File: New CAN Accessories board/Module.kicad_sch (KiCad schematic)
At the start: 11 parts, among them J1 39301040, Q1 IRLML6344TRPBF

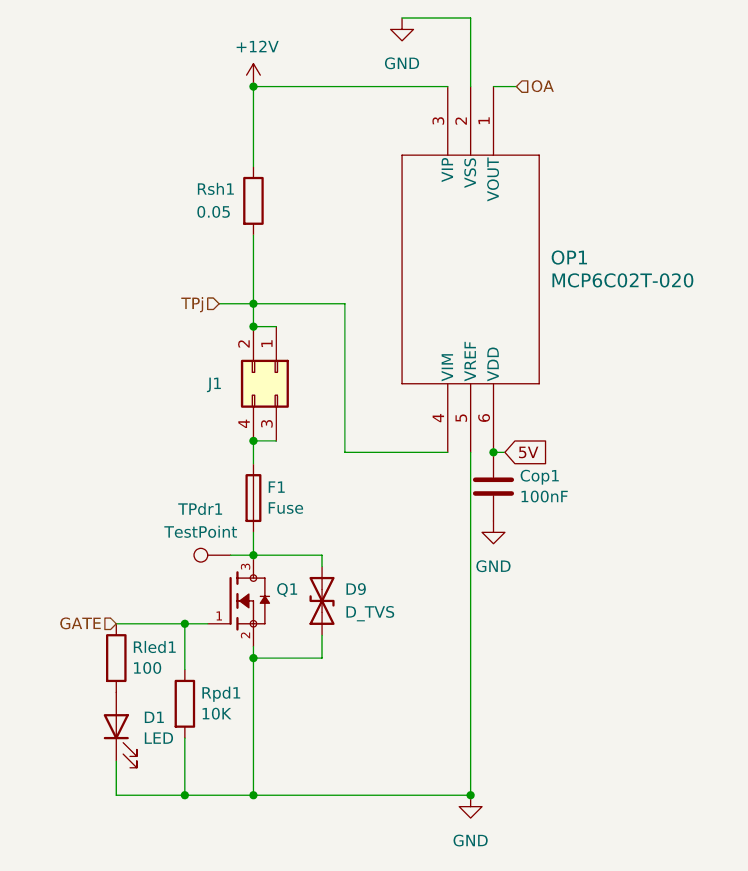
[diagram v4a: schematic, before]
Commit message: named tvs diode correctly
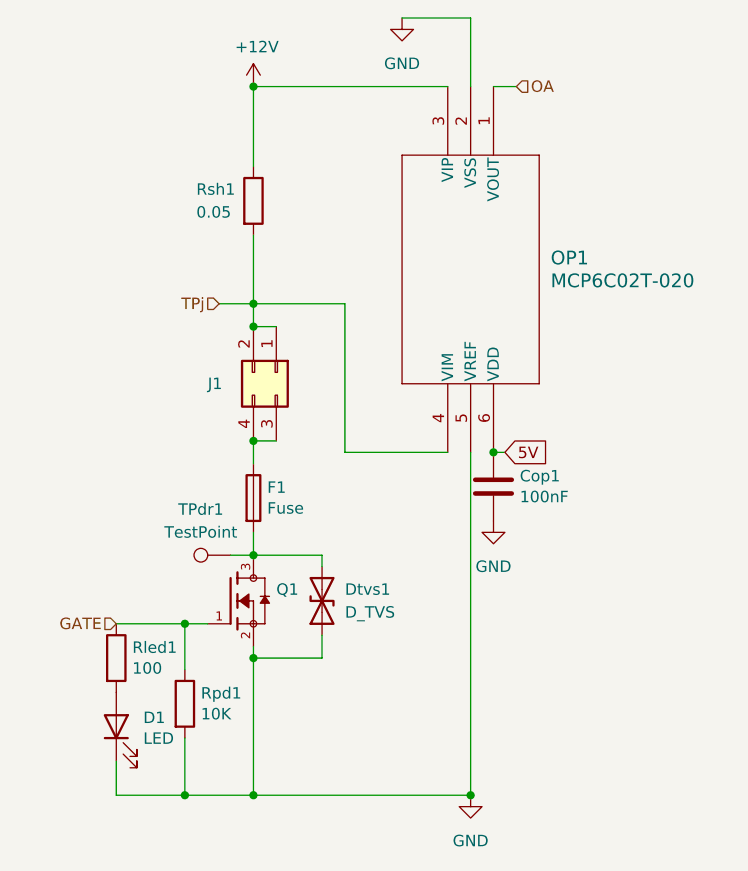
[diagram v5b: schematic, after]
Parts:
- removed D9: D_TVS, symbol Device:D_TVS
- added Dtvs1: D_TVS, symbol Device:D_TVS
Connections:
- net GND: now also Dtvs1.1 (A1)
- net at F1.2, Q1.3, TPdr1.1: now also Dtvs1.2 (A2)
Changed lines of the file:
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@@
-	(wire
-		(pts
-			(xy 48.26 76.2) (xy 48.26 77.47)
-		)
-		(stroke
-			(width 0)
-			(type default)
-		)
-	)
 	(wire
 		(pts
@@
 		(pts
 			(xy 48.26 85.09) (xy 48.26 87.63)
+		)
+		(stroke
+			(width 0)
+			(type default)
+		)
+	)
+	(wire
+		(pts
+			(xy 48.26 77.47) (xy 48.26 76.2)
 		)
 		(stroke
@@
 	)
 	(symbol
+		(lib_id "Device:D_TVS")
+		(at 48.26 81.28 90)
+		(unit 1)
+		(exclude_from_sim no)
+		(in_bom yes)
+		(on_board yes)
+		(dnp no)
+		(fields_autoplaced yes)
+		(property "Reference" "Dtvs1"
+			(at 50.8 80.0099 90)
+			(effects
+				(font
+					(size 1.27 1.27)
+				)
+				(justify right)
+			)
+		)
+		(property "Value" "D_TVS"
+			(at 50.8 82.5499 90)
+			(effects
+				(font
+					(size 1.27 1.27)
+				)
+				(justify right)
+			)
+		)
+		(property "Footprint" ""
+			(at 48.26 81.28 0)
+			(effects
+				(font
+					(size 1.27 1.27)
+				)
+				(hide yes)
+			)
+		)
+		(property "Datasheet" "~"
+			(at 48.26 81.28 0)
+			(effects
+				(font
+					(size 1.27 1.27)
+				)
+				(hide yes)
+			)
+		)
+		(property "Description" "Bidirectional transient-voltage-suppression diode"
+			(at 48.26 81.28 0)
+			(effects
+				(font
+					(size 1.27 1.27)
+				)
+				(hide yes)
+			)
+		)
+		(pin "2"
+		)
+		(pin "1"
+		)
+		(instances
+			(project "New CAN Accessories board"
+				(path "/88340f43-3f46-45a6-9393-130e00dc3071/066a2d54-ef62-4b50-bc17-9ae15f85282f"
+					(reference "Dtvs3")
+					(unit 1)
+				)
+				(path "/88340f43-3f46-45a6-9393-130e00dc3071/199d9661-d77c-40a8-9127-2f77ddd20cbc"
+					(reference "Dtvs2")
+					(unit 1)
+				)
+				(path "/88340f43-3f46-45a6-9393-130e00dc3071/a4a3a29c-d4d7-4a64-89ca-c4c515902e3a"
+					(reference "Dtvs8")
+					(unit 1)
+				)
+				(path "/88340f43-3f46-45a6-9393-130e00dc3071/b4fef664-0317-4528-b914-9a729a4fa0cb"
+					(reference "Dtvs7")
+					(unit 1)
+				)
+				(path "/88340f43-3f46-45a6-9393-130e00dc3071/df424b4d-8c7c-4d94-be97-d7e7a5882dfa"
+					(reference "Dtvs6")
+					(unit 1)
+				)
+				(path "/88340f43-3f46-45a6-9393-130e00dc3071/e28dd46e-a6b0-42fd-b358-90f6a987ac56"
+					(reference "Dtvs4")
+					(unit 1)
+				)
+				(path "/88340f43-3f46-45a6-9393-130e00dc3071/f4946d2d-97a8-44f8-9d9c-ff737967b4cd"
+					(reference "Dtvs5")
+					(unit 1)
+				)
+				(path "/88340f43-3f46-45a6-9393-130e00dc3071/fb19124a-c234-4595-adc5-bbb1e37c8292"
+					(reference "Dtvs1")
+					(unit 1)
+				)
+			)
+		)
+	)
+	(symbol
 		(lib_id "Device:R")
 		(at 33.02 92.71 0)
@@
 					(unit 1)
 				)
-			)
-		)
-	)
-	(symbol
-		(lib_id "Device:D_TVS")
-		(at 48.26 81.28 90)
-		(unit 1)
-		(exclude_from_sim no)
-		(in_bom yes)
-		(on_board yes)
-		(dnp no)
-		(fields_autoplaced yes)
-		(property "Reference" "D9"
-			(at 50.8 80.0099 90)
-			(effects
-				(font
-					(size 1.27 1.27)
-				)
-				(justify right)
-			)
-		)
-		(property "Value" "D_TVS"
-			(at 50.8 82.5499 90)
-			(effects
-				(font
-					(size 1.27 1.27)
-				)
-				(justify right)
-			)
-		)
-		(property "Footprint" ""
-			(at 48.26 81.28 0)
-			(effects
-				(font
-					(size 1.27 1.27)
-				)
-				(hide yes)
-			)
-		)
-		(property "Datasheet" "~"
-			(at 48.26 81.28 0)
-			(effects
-				(font
-					(size 1.27 1.27)
-				)
-				(hide yes)
-			)
-		)
-		(property "Description" "Bidirectional transient-voltage-suppression diode"
-			(at 48.26 81.28 0)
-			(effects
-				(font
-					(size 1.27 1.27)
-				)
-				(hide yes)
-			)
-		)
-		(pin "1"
-		)
-		(pin "2"
-		)
-		(instances
-			(project ""
-				(path "/88340f43-3f46-45a6-9393-130e00dc3071/066a2d54-ef62-4b50-bc17-9ae15f85282f"
-					(reference "D11")
-					(unit 1)
-				)
-				(path "/88340f43-3f46-45a6-9393-130e00dc3071/199d9661-d77c-40a8-9127-2f77ddd20cbc"
-					(reference "D10")
-					(unit 1)
-				)
-				(path "/88340f43-3f46-45a6-9393-130e00dc3071/a4a3a29c-d4d7-4a64-89ca-c4c515902e3a"
-					(reference "D16")
-					(unit 1)
-				)
-				(path "/88340f43-3f46-45a6-9393-130e00dc3071/b4fef664-0317-4528-b914-9a729a4fa0cb"
-					(reference "D15")
-					(unit 1)
-				)
-				(path "/88340f43-3f46-45a6-9393-130e00dc3071/df424b4d-8c7c-4d94-be97-d7e7a5882dfa"
-					(reference "D14")
-					(unit 1)
-				)
-				(path "/88340f43-3f46-45a6-9393-130e00dc3071/e28dd46e-a6b0-42fd-b358-90f6a987ac56"
-					(reference "D12")
-					(unit 1)
-				)
-				(path "/88340f43-3f46-45a6-9393-130e00dc3071/f4946d2d-97a8-44f8-9d9c-ff737967b4cd"
-					(reference "D13")
-					(unit 1)
-				)
-				(path "/88340f43-3f46-45a6-9393-130e00dc3071/fb19124a-c234-4595-adc5-bbb1e37c8292"
-					(reference "D9")
-					(unit 1)
-				)

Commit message: started making drain test point changes
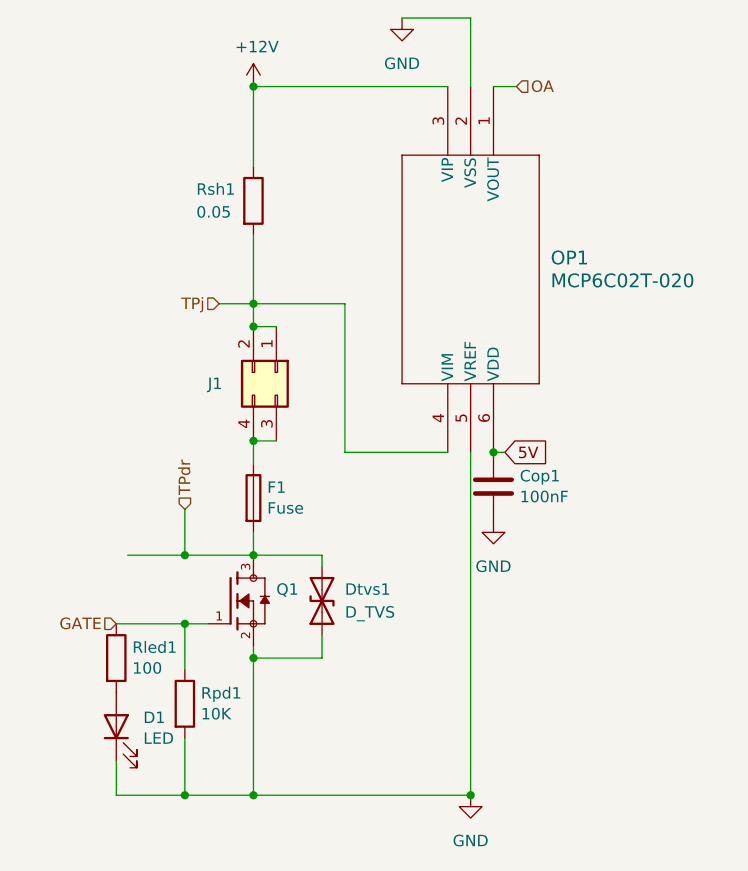
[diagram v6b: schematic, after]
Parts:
- removed TPdr1: TestPoint, Connector_PinHeader_2.54mm:PinHeader_1x01_P2.54mm_Vertical, symbol Connector:TestPoint
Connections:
- net TPdr: now reaches Dtvs1.2 (A2), F1.2, Q1.3
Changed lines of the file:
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@@
+	)
+	(junction
+		(at 33.02 76.2)
+		(diameter 0)
+		(color 0 0 0 0)
 	)
 	(junction
@@
 	(wire
 		(pts
+			(xy 33.02 76.2) (xy 40.64 76.2)
+		)
+		(stroke
+			(width 0)
+			(type default)
+		)
+	)
+	(wire
+		(pts
 			(xy 50.8 48.26) (xy 40.64 48.26)
 		)
@@
 	(wire
 		(pts
-			(xy 38.1 76.2) (xy 40.64 76.2)
+			(xy 26.67 76.2) (xy 33.02 76.2)
+		)
+		(stroke
+			(width 0)
+			(type default)
+		)
+	)
+	(wire
+		(pts
+			(xy 33.02 71.12) (xy 33.02 76.2)
 		)
 		(stroke
@@
 				(hide yes)
 			)
+		)
+	)
+	(hierarchical_label "TPdr"
+		(shape input)
+		(at 33.02 71.12 90)
+		(effects
+			(font
+				(size 1.27 1.27)
+			)
+			(justify left)
 		)
 	)
@@
 					(unit 1)
 				)
-			)
-		)
-	)
-	(symbol
-		(lib_id "Connector:TestPoint")
-		(at 38.1 76.2 90)
-		(unit 1)
-		(exclude_from_sim no)
-		(in_bom yes)
-		(on_board yes)
-		(dnp no)
-		(fields_autoplaced yes)
-		(property "Reference" "TPdr1"
-			(at 34.798 71.12 90)
-			(effects
-				(font
-					(size 1.27 1.27)
-				)
-			)
-		)
-		(property "Value" "TestPoint"
-			(at 34.798 73.66 90)
-			(effects
-				(font
-					(size 1.27 1.27)
-				)
-			)
-		)
-		(property "Footprint" "Connector_PinHeader_2.54mm:PinHeader_1x01_P2.54mm_Vertical"
-			(at 38.1 71.12 0)
-			(effects
-				(font
-					(size 1.27 1.27)
-				)
-				(hide yes)
-			)
-		)
-		(property "Datasheet" "~"
-			(at 38.1 71.12 0)
-			(effects
-				(font
-					(size 1.27 1.27)
-				)
-				(hide yes)
-			)
-		)
-		(property "Description" "test point"
-			(at 38.1 76.2 0)
-			(effects
-				(font
-					(size 1.27 1.27)
-				)
-				(hide yes)
-			)
-		)
-		(property "Purpose" ""
-			(at 38.1 76.2 0)
-			(effects
-				(font
-					(size 1.27 1.27)
-				)
-			)
-		)
-		(pin "1"
-		)
-		(instances
-			(project "New CAN Accessories board"
-				(path "/88340f43-3f46-45a6-9393-130e00dc3071/066a2d54-ef62-4b50-bc17-9ae15f85282f"
-					(reference "TPdr3")
-					(unit 1)
-				)
-				(path "/88340f43-3f46-45a6-9393-130e00dc3071/199d9661-d77c-40a8-9127-2f77ddd20cbc"
-					(reference "TPdr2")
-					(unit 1)
-				)
-				(path "/88340f43-3f46-45a6-9393-130e00dc3071/a4a3a29c-d4d7-4a64-89ca-c4c515902e3a"
-					(reference "TPdr8")
-					(unit 1)
-				)
-				(path "/88340f43-3f46-45a6-9393-130e00dc3071/b4fef664-0317-4528-b914-9a729a4fa0cb"
-					(reference "TPdr7")
-					(unit 1)
-				)
-				(path "/88340f43-3f46-45a6-9393-130e00dc3071/df424b4d-8c7c-4d94-be97-d7e7a5882dfa"
-					(reference "TPdr6")
-					(unit 1)
-				)
-				(path "/88340f43-3f46-45a6-9393-130e00dc3071/e28dd46e-a6b0-42fd-b358-90f6a987ac56"
-					(reference "TPdr4")
-					(unit 1)
-				)
-				(path "/88340f43-3f46-45a6-9393-130e00dc3071/f4946d2d-97a8-44f8-9d9c-ff737967b4cd"
-					(reference "TPdr5")
-					(unit 1)
-				)
-				(path "/88340f43-3f46-45a6-9393-130e00dc3071/fb19124a-c234-4595-adc5-bbb1e37c8292"
-					(reference "TPdr1")
-					(unit 1)
-				)

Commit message: 1x16 header test points
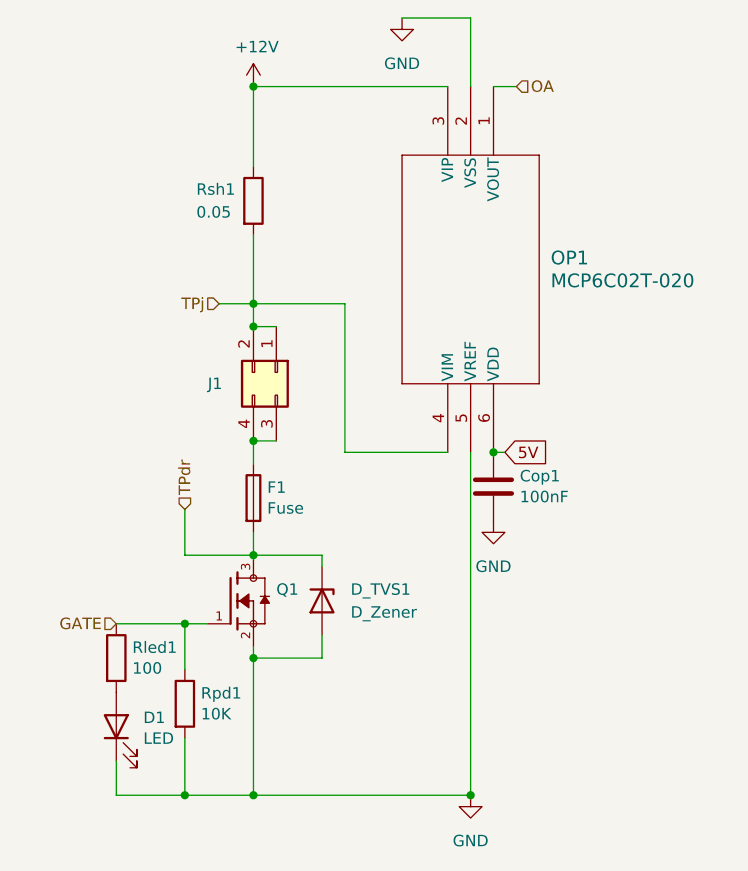
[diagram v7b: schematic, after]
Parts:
- removed Dtvs1: D_TVS, symbol Device:D_TVS
- added D_TVS1: D_Zener, Diode_SMD:D_SMF, symbol Device:D_Zener
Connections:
- net GND: now also D_TVS1.2 (A)
- net TPdr: now also D_TVS1.1 (K)
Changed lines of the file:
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@@
-	)
-	(junction
-		(at 33.02 76.2)
-		(diameter 0)
-		(color 0 0 0 0)
 	)
 	(junction
@@
 		(pts
 			(xy 69.85 24.13) (xy 67.31 24.13)
-		)
-		(stroke
-			(width 0)
-			(type default)
-		)
-	)
-	(wire
-		(pts
-			(xy 26.67 76.2) (xy 33.02 76.2)
 		)
 		(stroke
@@
 	)
 	(symbol
-		(lib_id "Device:D_TVS")
-		(at 48.26 81.28 90)
-		(unit 1)
-		(exclude_from_sim no)
-		(in_bom yes)
-		(on_board yes)
-		(dnp no)
-		(fields_autoplaced yes)
-		(property "Reference" "Dtvs1"
-			(at 50.8 80.0099 90)
-			(effects
-				(font
-					(size 1.27 1.27)
-				)
-				(justify right)
-			)
-		)
-		(property "Value" "D_TVS"
-			(at 50.8 82.5499 90)
-			(effects
-				(font
-					(size 1.27 1.27)
-				)
-				(justify right)
-			)
-		)
-		(property "Footprint" ""
-			(at 48.26 81.28 0)
-			(effects
-				(font
-					(size 1.27 1.27)
-				)
-				(hide yes)
-			)
-		)
-		(property "Datasheet" "~"
-			(at 48.26 81.28 0)
-			(effects
-				(font
-					(size 1.27 1.27)
-				)
-				(hide yes)
-			)
-		)
-		(property "Description" "Bidirectional transient-voltage-suppression diode"
-			(at 48.26 81.28 0)
-			(effects
-				(font
-					(size 1.27 1.27)
-				)
-				(hide yes)
-			)
-		)
-		(pin "2"
-		)
-		(pin "1"
-		)
-		(instances
-			(project "New CAN Accessories board"
-				(path "/88340f43-3f46-45a6-9393-130e00dc3071/066a2d54-ef62-4b50-bc17-9ae15f85282f"
-					(reference "Dtvs3")
-					(unit 1)
-				)
-				(path "/88340f43-3f46-45a6-9393-130e00dc3071/199d9661-d77c-40a8-9127-2f77ddd20cbc"
-					(reference "Dtvs2")
-					(unit 1)
-				)
-				(path "/88340f43-3f46-45a6-9393-130e00dc3071/a4a3a29c-d4d7-4a64-89ca-c4c515902e3a"
-					(reference "Dtvs8")
-					(unit 1)
-				)
-				(path "/88340f43-3f46-45a6-9393-130e00dc3071/b4fef664-0317-4528-b914-9a729a4fa0cb"
-					(reference "Dtvs7")
-					(unit 1)
-				)
-				(path "/88340f43-3f46-45a6-9393-130e00dc3071/df424b4d-8c7c-4d94-be97-d7e7a5882dfa"
-					(reference "Dtvs6")
-					(unit 1)
-				)
-				(path "/88340f43-3f46-45a6-9393-130e00dc3071/e28dd46e-a6b0-42fd-b358-90f6a987ac56"
-					(reference "Dtvs4")
-					(unit 1)
-				)
-				(path "/88340f43-3f46-45a6-9393-130e00dc3071/f4946d2d-97a8-44f8-9d9c-ff737967b4cd"
-					(reference "Dtvs5")
-					(unit 1)
-				)
-				(path "/88340f43-3f46-45a6-9393-130e00dc3071/fb19124a-c234-4595-adc5-bbb1e37c8292"
-					(reference "Dtvs1")
-					(unit 1)
-				)
-			)
-		)
-	)
-	(symbol
 		(lib_id "Device:R")
 		(at 33.02 92.71 0)
@@
 					(unit 1)
 				)
+			)
+		)
+	)
+	(symbol
+		(lib_id "Device:D_Zener")
+		(at 48.26 81.28 270)
+		(unit 1)
+		(exclude_from_sim no)
+		(in_bom yes)
+		(on_board yes)
+		(dnp no)
+		(fields_autoplaced yes)
+		(property "Reference" "D_TVS1"
+			(at 51.435 80.0099 90)
+			(effects
+				(font
+					(size 1.27 1.27)
+				)
+				(justify left)
+			)
+		)
+		(property "Value" "D_Zener"
+			(at 51.435 82.5499 90)
+			(effects
+				(font
+					(size 1.27 1.27)
+				)
+				(justify left)
+			)
+		)
+		(property "Footprint" "Diode_SMD:D_SMF"
+			(at 48.26 81.28 0)
+			(effects
+				(font
+					(size 1.27 1.27)
+				)
+				(hide yes)
+			)
+		)
+		(property "Datasheet" "~"
+			(at 48.26 81.28 0)
+			(effects
+				(font
+					(size 1.27 1.27)
+				)
+				(hide yes)
+			)
+		)
+		(property "Description" "Zener diode"
+			(at 48.26 81.28 0)
+			(effects
+				(font
+					(size 1.27 1.27)
+				)
+				(hide yes)
+			)
+		)
+		(property "Purpose" ""
+			(at 48.26 81.28 0)
+			(effects
+				(font
+					(size 1.27 1.27)
+				)
+			)
+		)
+		(pin "1"
+		)
+		(pin "2"
+		)
+		(instances
+			(project "New CAN Accessories board"
+				(path "/88340f43-3f46-45a6-9393-130e00dc3071/066a2d54-ef62-4b50-bc17-9ae15f85282f"
+					(reference "D_TVS3")
+					(unit 1)
+				)
+				(path "/88340f43-3f46-45a6-9393-130e00dc3071/199d9661-d77c-40a8-9127-2f77ddd20cbc"
+					(reference "D_TVS2")
+					(unit 1)
+				)
+				(path "/88340f43-3f46-45a6-9393-130e00dc3071/a4a3a29c-d4d7-4a64-89ca-c4c515902e3a"
+					(reference "D_TVS8")
+					(unit 1)
+				)
+				(path "/88340f43-3f46-45a6-9393-130e00dc3071/b4fef664-0317-4528-b914-9a729a4fa0cb"
+					(reference "D_TVS7")
+					(unit 1)
+				)
+				(path "/88340f43-3f46-45a6-9393-130e00dc3071/df424b4d-8c7c-4d94-be97-d7e7a5882dfa"
+					(reference "D_TVS6")
+					(unit 1)
+				)
+				(path "/88340f43-3f46-45a6-9393-130e00dc3071/e28dd46e-a6b0-42fd-b358-90f6a987ac56"
+					(reference "D_TVS4")
+					(unit 1)
+				)
+				(path "/88340f43-3f46-45a6-9393-130e00dc3071/f4946d2d-97a8-44f8-9d9c-ff737967b4cd"
+					(reference "D_TVS5")
+					(unit 1)
+				)
+				(path "/88340f43-3f46-45a6-9393-130e00dc3071/fb19124a-c234-4595-adc5-bbb1e37c8292"
+					(reference "D_TVS1")
+					(unit 1)
+				)
